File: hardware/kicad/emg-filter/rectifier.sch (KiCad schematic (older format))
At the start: 128 parts, among them U36 LM4565, U37 LM4565, U38 LM4565, U39 LM4565, U40 LM4565, U41 LM4565, U42 LM4565, U43 LM4565, U44 LM4565, U45 LM4565, U46 LM4565, U47 LM4565, U48 LM4565, U49 LM4565, U50 LM4565, U51 LM4565

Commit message: Manual Merged of Rectifier Review to Main
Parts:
- removed D10, D11, D12, D13, D14, D15, D16, D17, D18, D19, D20, D21, D22, D23, D24, D25, D26, D27, D28, D29, D30, D31, D32, D33, D34, D35, D36, D37, D38, D7, D8, D9: 1N4148, symbol Device:D
- removed R155, R156, R157, R158, R159, R160, R161, R162, R163, R164, R165, R166, R167, R168, R169, R170, R172, R174, R176, R178, R180, R182, R184, R186, R187, R188, R189, R190, R191, R192, R193, R194, R195, R196, R197, R198, R199, R200, R201, R202, R203, R204, R205, R206, R207, R208, R209, R210, R212, R214, R216, R218, R220, R222, R224, R226, R227, R228, R229, R230, R231, R232, R233, R234: 10k, symbol Device:R
- removed R171, R173, R175, R177, R179, R181, R183, R185, R211, R213, R215, R217, R219, R221, R223, R225: 5k, symbol Device:R
- removed U36, U37, U38, U39, U40, U41, U42, U43, U44, U45, U46, U47, U48, U49, U50, U51: LM4565, symbol emg-filter:LM4565
- added C? (x16): 0.1u, symbol Device:C
- added D? (x16): 1N4148, symbol Device:D
- added R? (x32): 10k, symbol Device:R
- added R? (x8): 5k, symbol Device:R
- added U? (x8): LM4565, symbol emg-filter:LM4565
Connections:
- net +5V: now also C?.1, C?.1, C?.1, C?.1, C?.1, C?.1, C?.1, C?.1, U?.8 (VCC), U?.8 (VCC), U?.8 (VCC), U?.8 (VCC), U?.8 (VCC), U?.8 (VCC), U?.8 (VCC), U?.8 (VCC)
- net -5V: now also C?.1, C?.1, C?.1, C?.1, C?.1, C?.1, C?.1, C?.1, U?.4 (VEE), U?.4 (VEE), U?.4 (VEE), U?.4 (VEE), U?.4 (VEE), U?.4 (VEE), U?.4 (VEE), U?.4 (VEE)
- net GND: now also C?.2, C?.2, C?.2, C?.2, C?.2, C?.2, C?.2, C?.2, C?.2, C?.2, C?.2, C?.2, C?.2, C?.2, C?.2, C?.2, D?.1 (K), D?.1 (K), R?.2, R?.2, R?.2, R?.2, U?.2 (-IN1), U?.2 (-IN1), U?.3 (+IN1), U?.3 (+IN1), U?.3 (+IN1), U?.3 (+IN1), U?.3 (+IN1), U?.3 (+IN1), U?.3 (+IN1), U?.3 (+IN1), U?.5 (+IN2), U?.5 (+IN2), U?.5 (+IN2), U?.5 (+IN2), U?.5 (+IN2), U?.5 (+IN2), U?.5 (+IN2), U?.5 (+IN2)
- net NOTCH_RECT_1: now also R?.1, R?.2
- net NOTCH_RECT_2: now also R?.1, R?.2
- net NOTCH_RECT_3: now also R?.1, R?.2
- net NOTCH_RECT_4: now also R?.1, R?.2
- net NOTCH_RECT_5: now also R?.1, R?.2
- net NOTCH_RECT_6: now also R?.1, R?.2
- net NOTCH_RECT_7: now also R?.1, R?.2
- net NOTCH_RECT_8: now also R?.1, R?.2
- new net: D?.2 (A), R?.1, R?.1 (x8)
- new net: R?.1, R?.2, R?.2, U?.6 (-IN2) (x8)
- new net: D?.1 (K), D?.2 (A), U?.1 (OUT1) (x8)
- new net: D?.1 (K), R?.2, R?.2, U?.2 (-IN1) (x6)
- new net RECT_AMP_1: R?.1, U?.7 (OUT2)
- new net RECT_AMP_2: R?.1, U?.7 (OUT2)
- new net RECT_AMP_3: R?.1, U?.7 (OUT2)
- new net RECT_AMP_4: R?.1, U?.7 (OUT2)
- new net RECT_AMP_5: R?.1, U?.7 (OUT2)
- new net RECT_AMP_6: R?.1, U?.7 (OUT2)
- new net RECT_AMP_7: R?.1, U?.7 (OUT2)
- new net RECT_AMP_8: R?.1, U?.7 (OUT2)

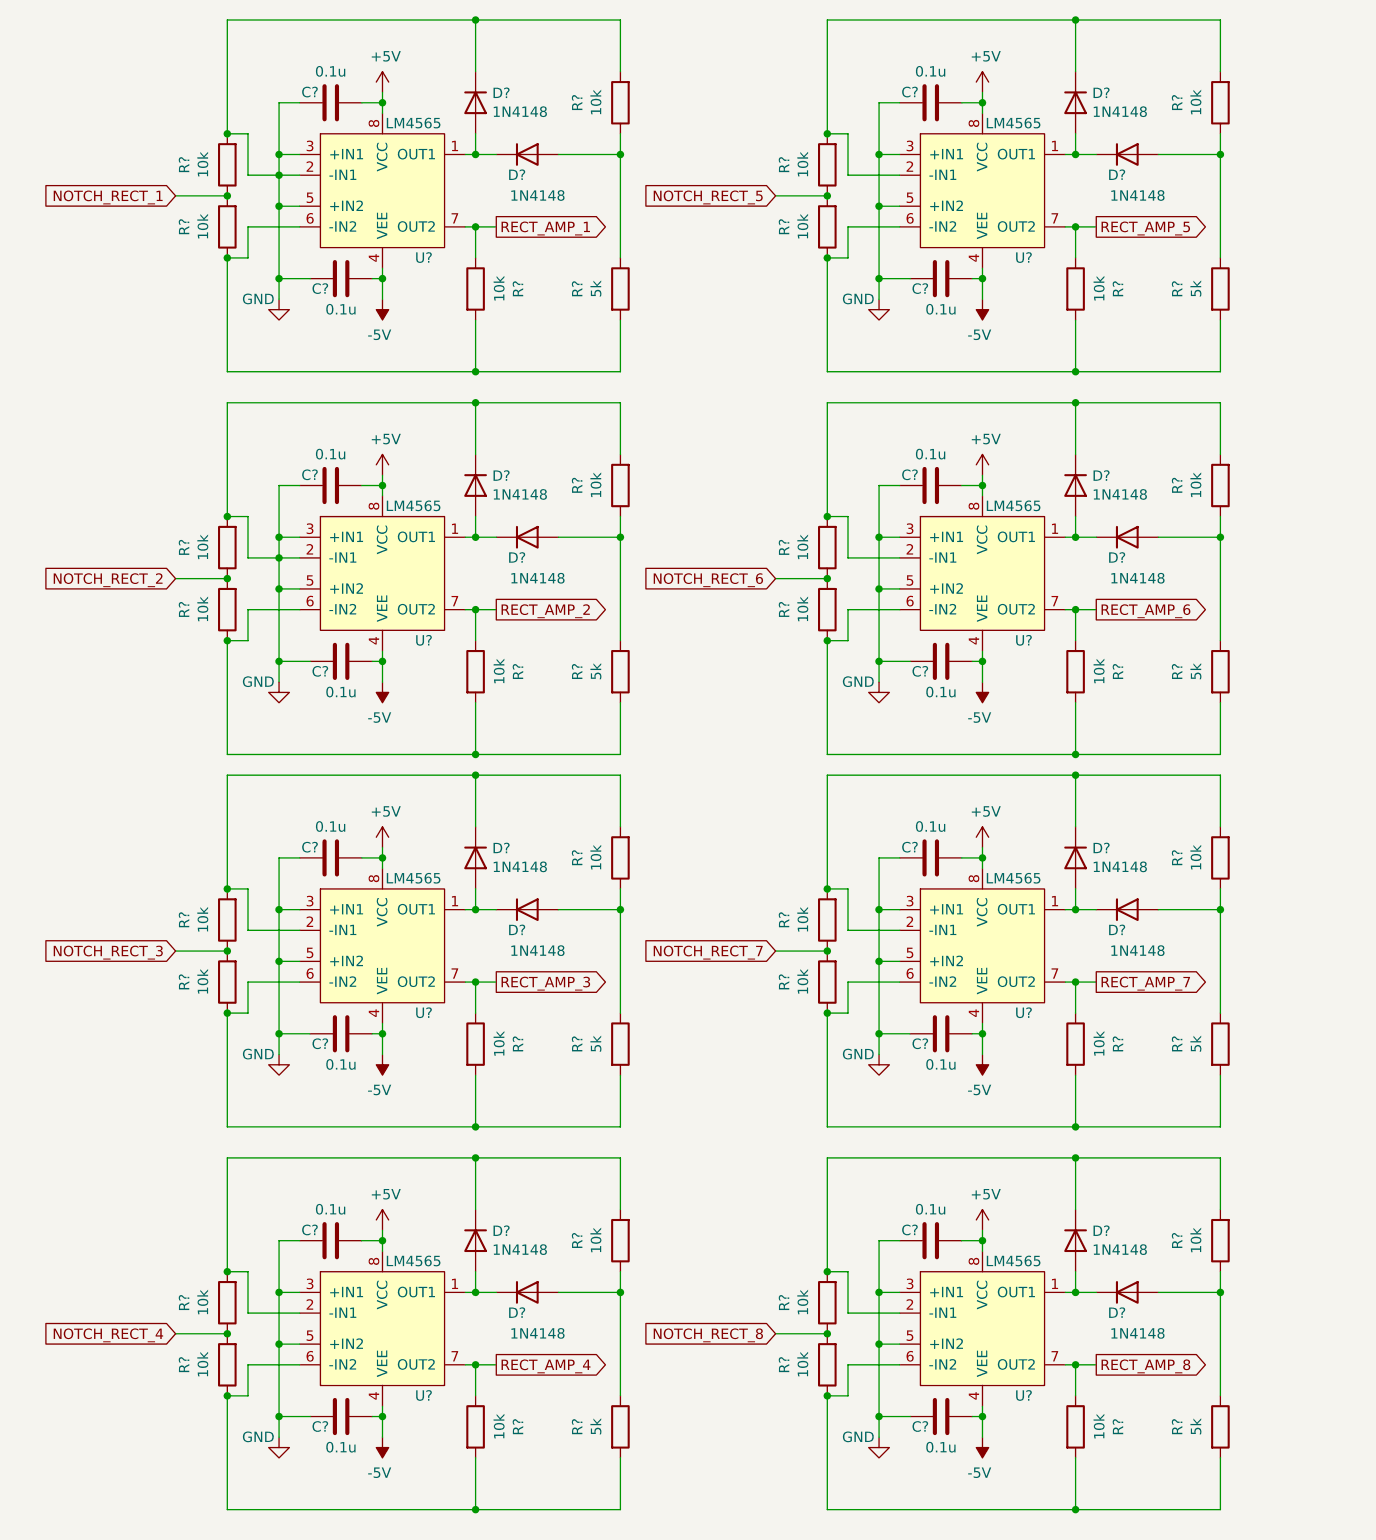
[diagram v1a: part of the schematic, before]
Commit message: fixed rectifier
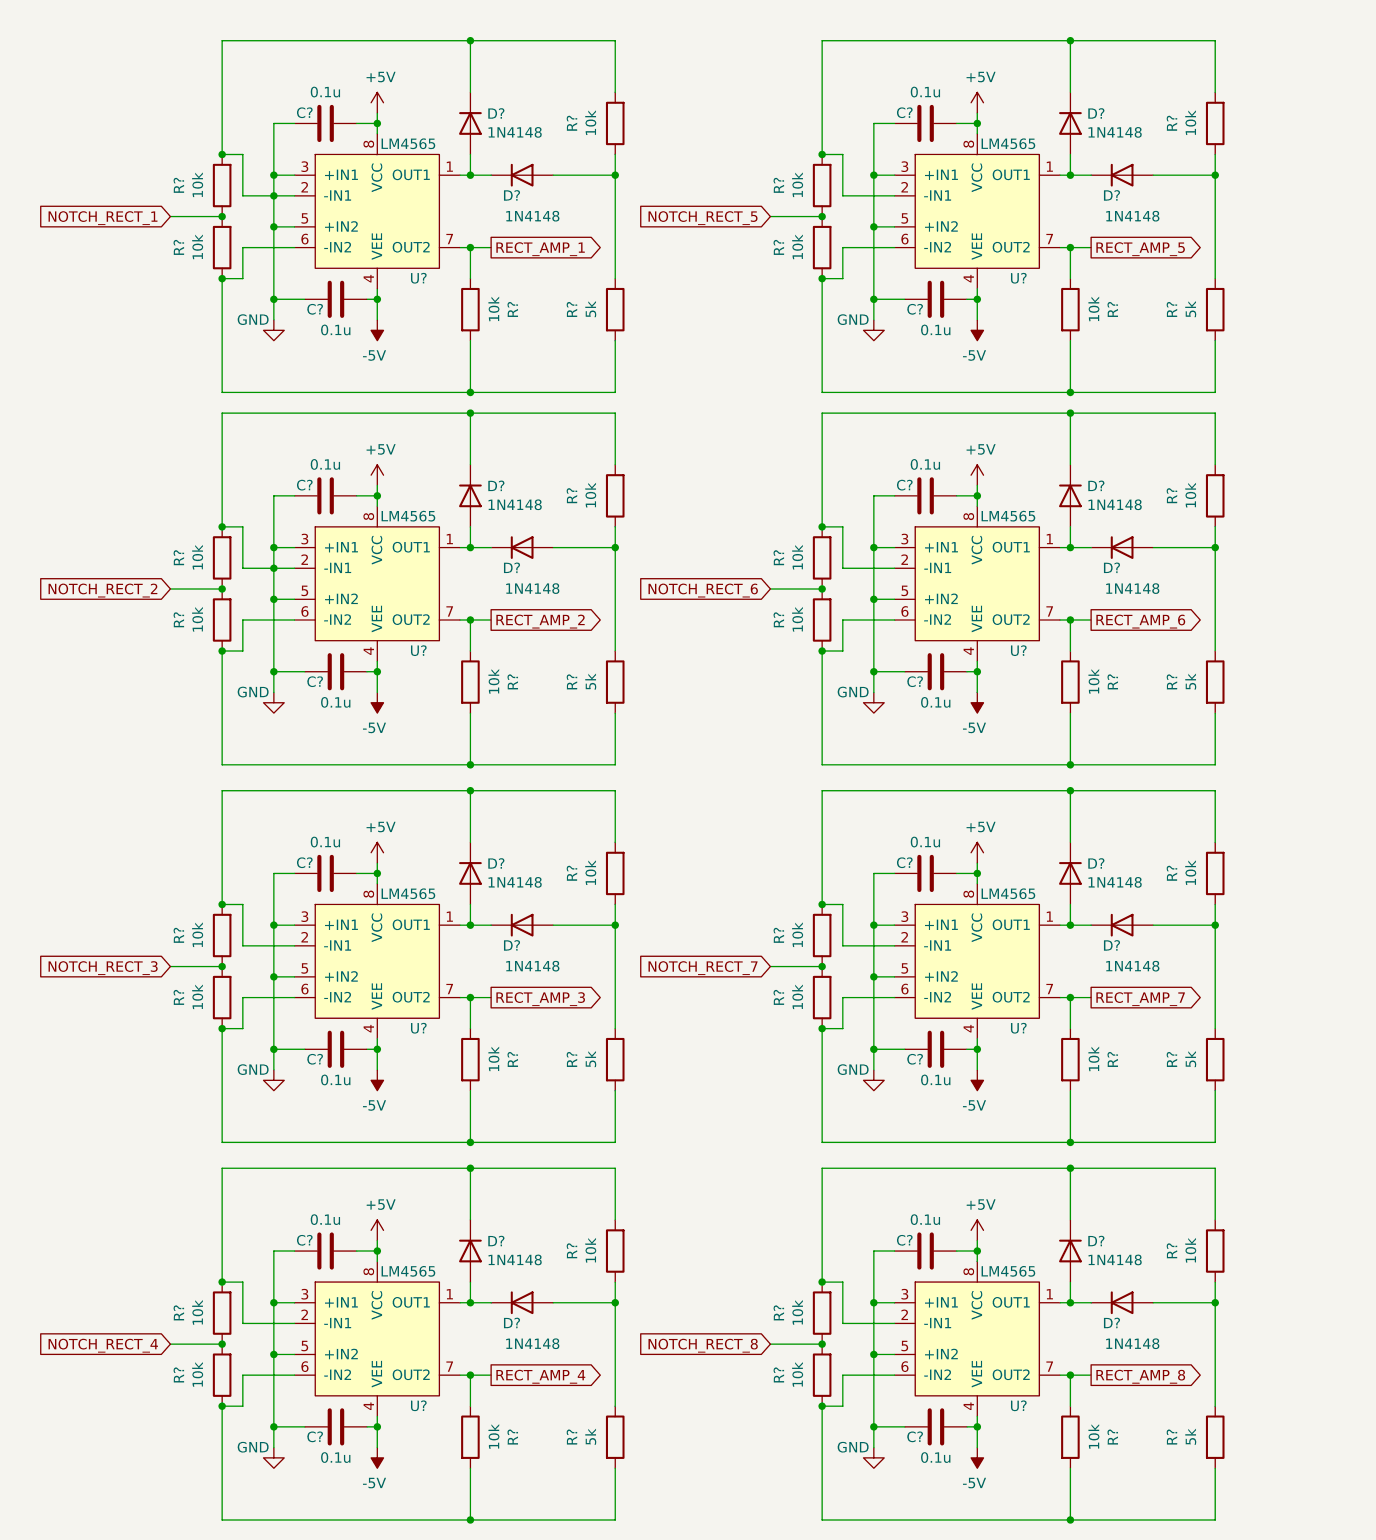
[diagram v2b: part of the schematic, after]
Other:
- moved on the sheet: C?, D?, R?, U?

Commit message: Connector
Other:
- moved on the sheet: C?, D?, R?, U?

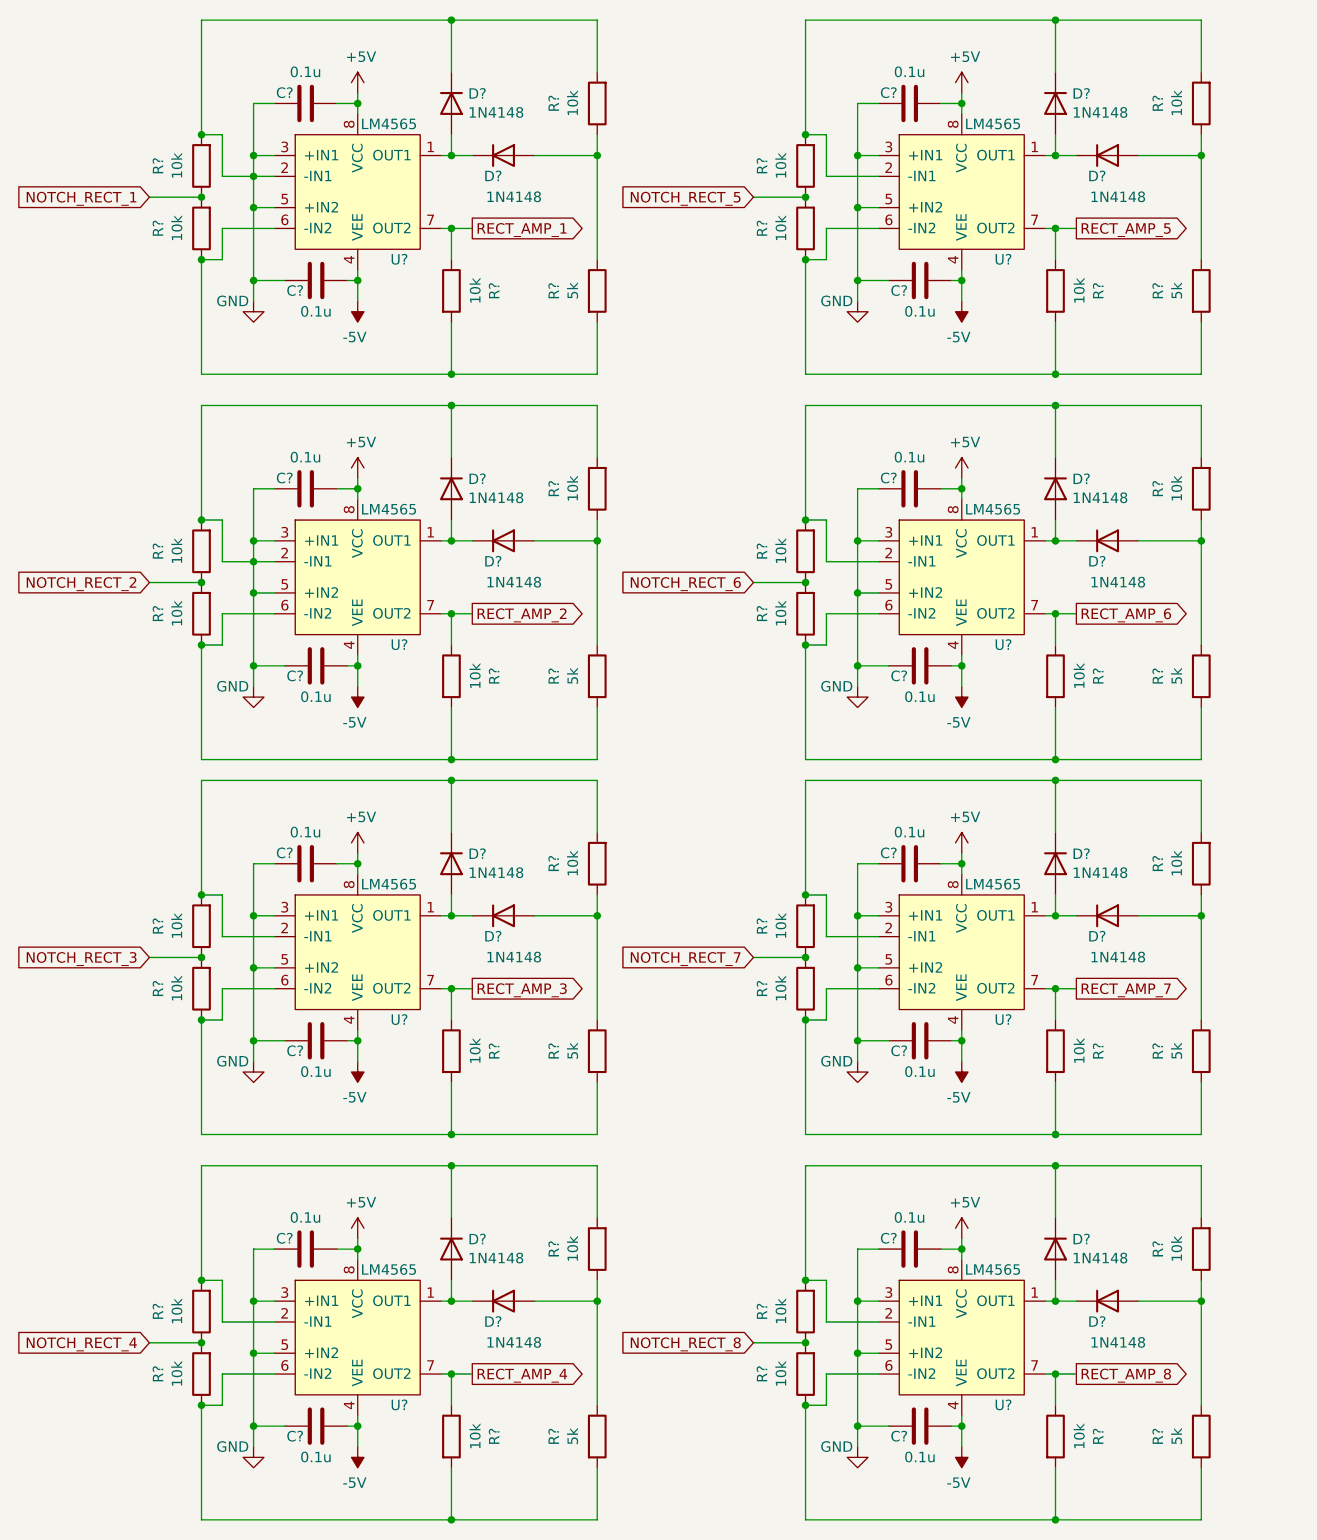
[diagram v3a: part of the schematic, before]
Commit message: fixed rect labels
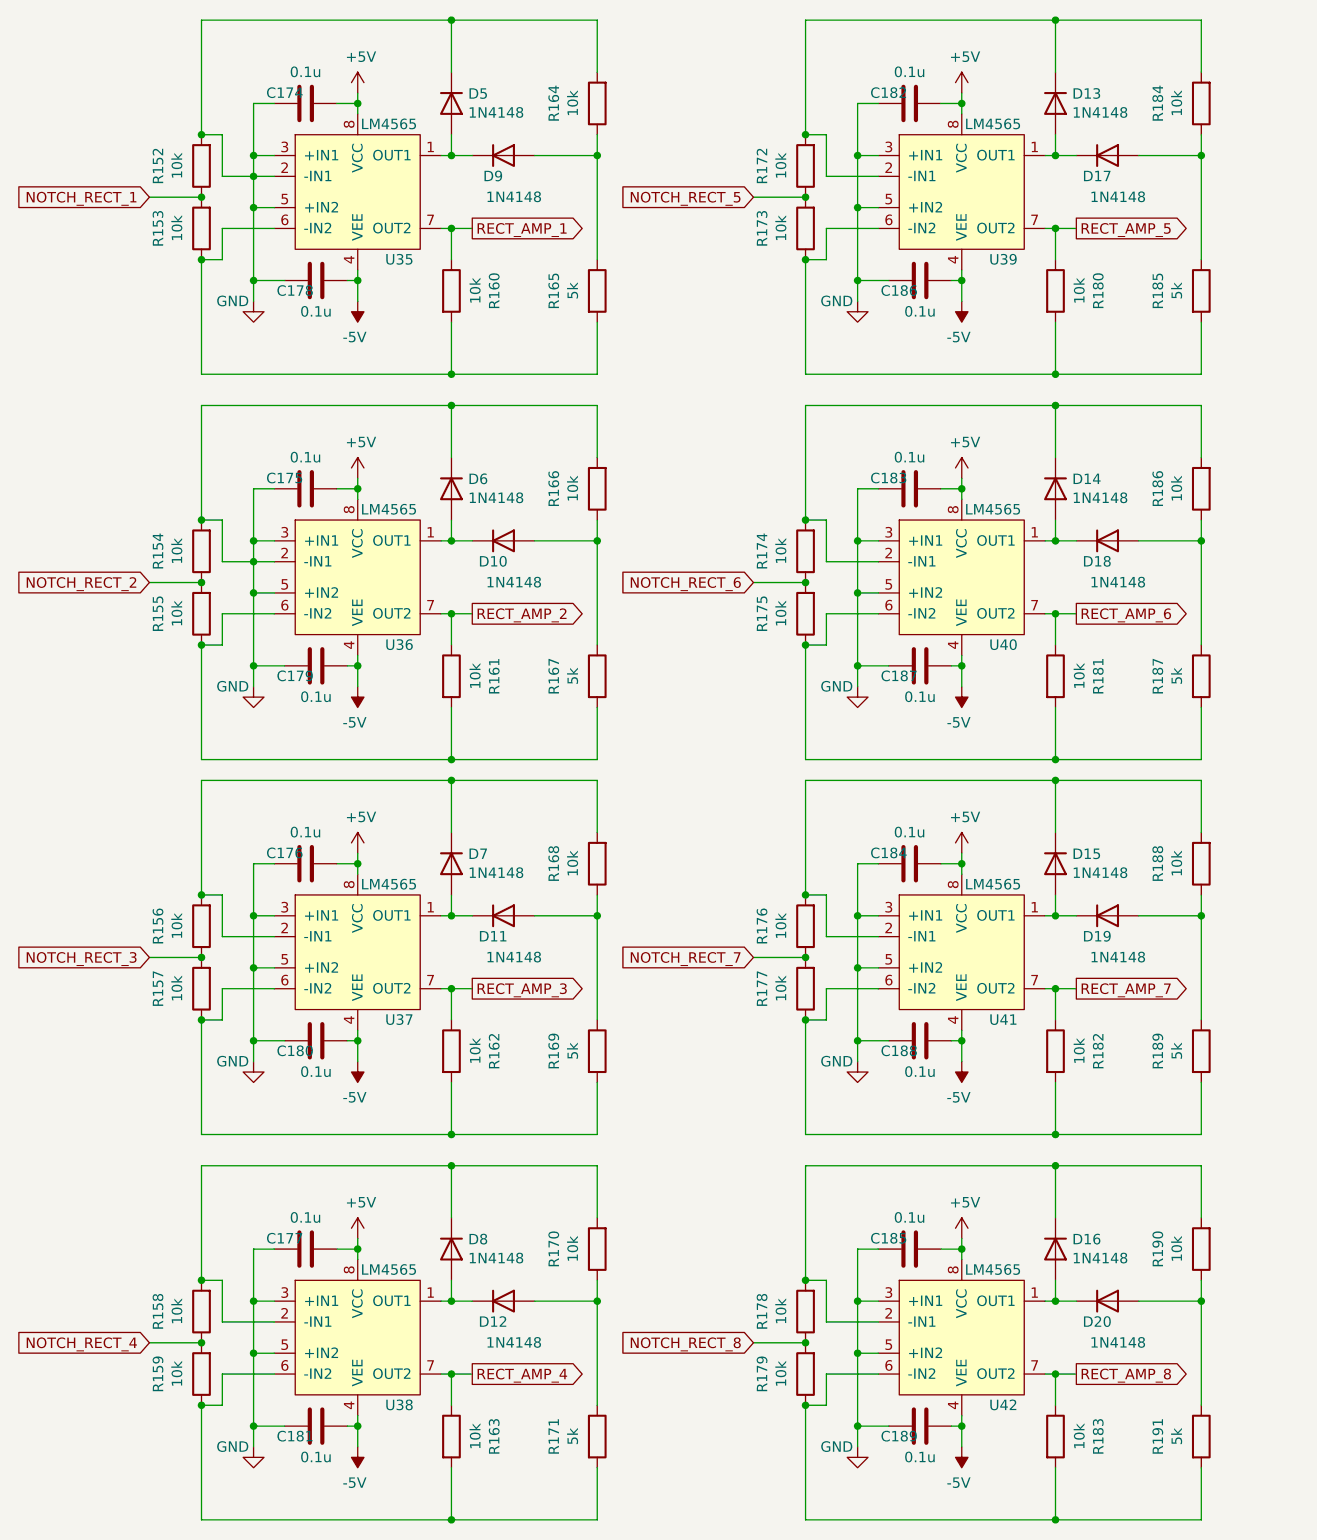
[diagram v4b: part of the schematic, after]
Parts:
- gave numbers to parts that had none: 80
